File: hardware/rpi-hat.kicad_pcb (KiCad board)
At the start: 2 copper layers, 65 x 56 mm, 86 parts, among them J1 Conn_02x20_Odd_Even__Rpi, J10 A1, J11 A2, J12 A3, J13 A4, J14 A5, J15 Alert, J16 Conn_01x02_Male, J16 I2C 5V, J17 PPS, J2 USART, J3 Jumper, J4 Fan 1, J5 Fan 2, J6 I2C 3.3V, J7 10103594-0001LF, J8 I2C 3.3V, J9 A0, U1 EEPROM, U10 5V, U11 3.3V -> 5V, U2 FAN, U3 BUF, U4 BSS138, U5 BSS138, U6 BUF, U7 DAC, U8 MUX, U9 ADC

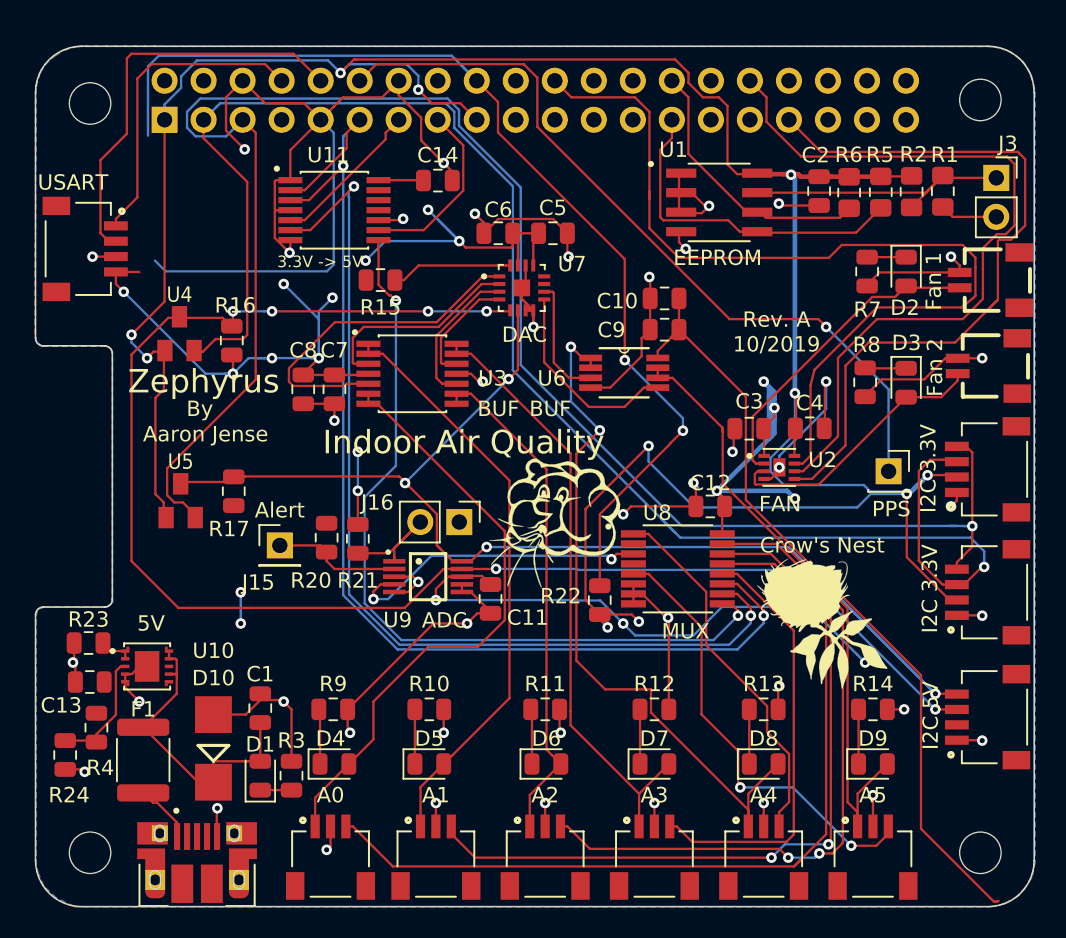
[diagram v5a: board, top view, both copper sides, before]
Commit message: Update silk screen
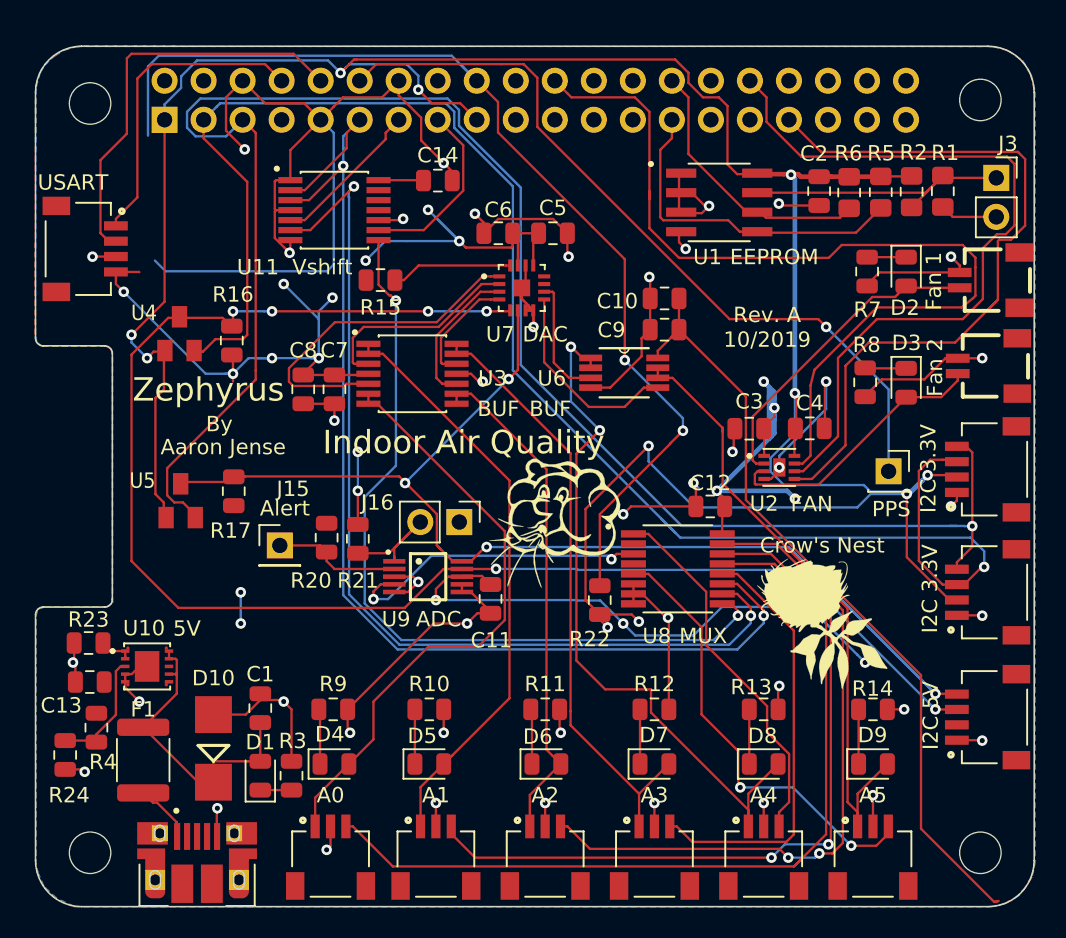
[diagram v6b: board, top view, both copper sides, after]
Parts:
- U11: value 3.3V -> 5V -> Vshift
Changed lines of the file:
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@@
   (layers
     (0 F.Cu signal hide)
-    (31 B.Cu signal hide)
+    (31 B.Cu signal)
     (32 B.Adhes user)
     (33 F.Adhes user)
-    (34 B.Paste user hide)
+    (34 B.Paste user)
     (35 F.Paste user)
     (36 B.SilkS user hide)
@@
     (at 209.4484 123.5788)
     (attr smd)
-    (fp_text reference U5 (at 0 -2.54) (layer F.SilkS)
+    (fp_text reference U5 (at -2.4892 -1.3032) (layer F.SilkS)
       (effects (font (size 1 0.9) (thickness 0.15)))
     )
@@
     (at 244.5004 104.1654)
     (attr smd)
-    (fp_text reference U1 (at -2.9718 -3.429) (layer F.SilkS)
+    (fp_text reference U1 (at -0.762 3.556) (layer F.SilkS)
       (effects (font (size 1 1) (thickness 0.15)))
     )
-    (fp_text value EEPROM (at -0.1016 3.6068) (layer F.SilkS)
+    (fp_text value EEPROM (at 3.5814 3.556) (layer F.SilkS)
       (effects (font (size 1 1) (thickness 0.15)))
     )
@@
     (at 248.412 121.412)
     (attr smd)
-    (fp_text reference U2 (at 2.8194 -0.4826) (layer F.SilkS)
+    (fp_text reference U2 (at -0.9906 2.3622) (layer F.SilkS)
       (effects (font (size 1 1) (thickness 0.15)))
     )
-    (fp_text value FAN (at 0.0508 2.3876) (layer F.SilkS)
+    (fp_text value FAN (at 2.1082 2.3876) (layer F.SilkS)
       (effects (font (size 1 1) (thickness 0.15)))
     )
@@
     (at 209.3722 112.7076)
     (attr smd)
-    (fp_text reference U4 (at 0 -2.54) (layer F.SilkS)
+    (fp_text reference U4 (at -2.3114 -1.354) (layer F.SilkS)
       (effects (font (size 1 0.9) (thickness 0.15)))
     )
@@
     (tags resistor)
     (attr smd)
-    (fp_text reference R17 (at -2.4638 -0.3048 180) (layer F.SilkS)
+    (fp_text reference R17 (at -2.5654 -0.2032 180) (layer F.SilkS)
       (effects (font (size 1 1) (thickness 0.15)))
     )
@@
     (tags resistor)
     (attr smd)
-    (fp_text reference R16 (at 2.2837 0.2286 180) (layer F.SilkS)
+    (fp_text reference R16 (at 2.9949 0.0762 180) (layer F.SilkS)
       (effects (font (size 1 1) (thickness 0.15)))
     )
@@
     (tags "resistor handsolder")
     (attr smd)
-    (fp_text reference R6 (at -2.4548 0.0254 180) (layer F.SilkS)
+    (fp_text reference R6 (at -2.5564 0.0508 180) (layer F.SilkS)
       (effects (font (size 1 1) (thickness 0.15)))
     )
@@
     (tags "resistor handsolder")
     (attr smd)
-    (fp_text reference R5 (at -2.4294 0.0508 180) (layer F.SilkS)
+    (fp_text reference R5 (at -2.531 -0.0254 180) (layer F.SilkS)
       (effects (font (size 1 1) (thickness 0.15)))
     )
@@
     (tags "resistor handsolder")
     (attr smd)
-    (fp_text reference R2 (at 2.3966 -1.905 180) (layer F.SilkS)
+    (fp_text reference R2 (at 2.5236 -1.905 180) (layer F.SilkS)
       (effects (font (size 1 1) (thickness 0.15)))
     )
@@
     (tags "resistor handsolder")
     (attr smd)
-    (fp_text reference R1 (at -2.3966 -2.159 180) (layer F.SilkS)
+    (fp_text reference R1 (at -2.5236 -2.1844 180) (layer F.SilkS)
       (effects (font (size 1 1) (thickness 0.15)))
     )
@@
     (tags capacitor)
     (attr smd)
-    (fp_text reference C2 (at -2.3345 0.2286 180) (layer F.SilkS)
+    (fp_text reference C2 (at -2.4361 0.3302 180) (layer F.SilkS)
       (effects (font (size 1 1) (thickness 0.15)))
     )
@@
     (at 219.457 104.668)
     (attr smd)
-    (fp_text reference U11 (at -0.41042 -3.58362) (layer F.SilkS)
+    (fp_text reference U11 (at -4.9794 3.7138) (layer F.SilkS)
       (effects (font (size 1 1) (thickness 0.15)))
     )
-    (fp_text value "3.3V -> 5V" (at -0.9408 3.3582) (layer F.SilkS)
-      (effects (font (size 0.75 0.75) (thickness 0.15)))
+    (fp_text value Vshift (at -0.7884 3.7138) (layer F.SilkS)
+      (effects (font (size 1 1) (thickness 0.15)))
     )
     (fp_line (start -4 2.75) (end -4 -2.75) (layer Eco1.User) (width 0.05))
@@
     (at 207.264 134.366)
     (attr smd)
-    (fp_text reference U10 (at 4.318 -1.016) (layer F.SilkS)
+    (fp_text reference U10 (at -0.2032 -2.4892) (layer F.SilkS)
       (effects (font (size 1 1) (thickness 0.15)))
     )
-    (fp_text value 5V (at 0.254 -2.794) (layer F.SilkS)
+    (fp_text value 5V (at 2.5908 -2.4638) (layer F.SilkS)
       (effects (font (size 1 1) (thickness 0.15)))
     )
@@
     (tags resistor)
     (attr smd)
-    (fp_text reference R4 (at 2.6185 -0.254 180) (layer F.SilkS)
+    (fp_text reference R4 (at 2.2375 -0.4318 180) (layer F.SilkS)
       (effects (font (size 1 1) (thickness 0.15)))
     )
@@
     (tags resistor)
     (attr smd)
-    (fp_text reference R3 (at 2.286 0 180) (layer F.SilkS)
+    (fp_text reference R3 (at 2.2606 0.0762 180) (layer F.SilkS)
       (effects (font (size 1 1) (thickness 0.15)))
     )
@@
     (tags diode)
     (attr smd)
-    (fp_text reference D1 (at 2.032 0 180) (layer F.SilkS)
+    (fp_text reference D1 (at 2.1844 0 180) (layer F.SilkS)
       (effects (font (size 1 1) (thickness 0.15)))
     )
@@
     (at 225.552 128.524)
     (attr smd)
-    (fp_text reference U9 (at -1.9812 2.8194) (layer F.SilkS)
+    (fp_text reference U9 (at -2.0828 2.7686) (layer F.SilkS)
       (effects (font (size 1 1) (thickness 0.15)))
     )
-    (fp_text value ADC (at 1.0668 2.8448) (layer F.SilkS)
+    (fp_text value ADC (at 0.6858 2.7686) (layer F.SilkS)
       (effects (font (size 1 1) (thickness 0.15)))
     )
@@
     (at 241.808 128.016)
     (attr smd)
-    (fp_text reference U8 (at -1.34 -3.647) (layer F.SilkS)
+    (fp_text reference U8 (at -1.3716 4.3688) (layer F.SilkS)
       (effects (font (size 1 1) (thickness 0.15)))
     )
-    (fp_text value MUX (at 0.508 4.064) (layer F.SilkS)
+    (fp_text value MUX (at 1.651 4.3688) (layer F.SilkS)
       (effects (font (size 1 1) (thickness 0.15)))
     )
@@
     (at 231.648 109.728)
     (attr smd)
-    (fp_text reference U7 (at 3.2766 -1.5494) (layer F.SilkS)
+    (fp_text reference U7 (at -1.397 3.0226) (layer F.SilkS)
       (effects (font (size 1 1) (thickness 0.15)))
     )
-    (fp_text value DAC (at 0.1778 3.048) (layer F.SilkS)
+    (fp_text value DAC (at 1.524 3.0226) (layer F.SilkS)
       (effects (font (size 1 1) (thickness 0.15)))
     )
@@
     (tags resistor)
     (attr smd)
-    (fp_text reference R22 (at 0.254 -2.54 180) (layer F.SilkS)
+    (fp_text reference R22 (at -2.54 -0.6604 180) (layer F.SilkS)
       (effects (font (size 1 1) (thickness 0.15)))
     )
@@
     (tags resistor)
     (attr smd)
-    (fp_text reference R14 (at 0 -1.65) (layer F.SilkS)
+    (fp_text reference R14 (at -0.0254 -1.3462) (layer F.SilkS)
       (effects (font (size 1 1) (thickness 0.15)))
     )
@@
     (tags resistor)
     (attr smd)
-    (fp_text reference R13 (at 0 -1.65) (layer F.SilkS)
+    (fp_text reference R13 (at -0.8128 -1.4478) (layer F.SilkS)
       (effects (font (size 1 1) (thickness 0.15)))
     )
@@
     (descr "Through hole straight pin header, 1x01, 2.54mm pitch, single row")
     (tags "Through hole pin header THT 1x01 2.54mm single row")
-    (fp_text reference J15 (at -1.397 2.413) (layer F.SilkS)
+    (fp_text reference J15 (at 0.8636 -3.683) (layer F.SilkS)
       (effects (font (size 1 1) (thickness 0.15)))
     )
@@
     (tags diode)
     (attr smd)
-    (fp_text reference D9 (at 0 -1.65) (layer F.SilkS)
+    (fp_text reference D9 (at -0.0254 -1.8796) (layer F.SilkS)
       (effects (font (size 1 1) (thickness 0.15)))
     )
@@
     (tags diode)
     (attr smd)
-    (fp_text reference D8 (at 0 -1.65) (layer F.SilkS)
+    (fp_text reference D8 (at -0.0762 -1.8288) (layer F.SilkS)
       (effects (font (size 1 1) (thickness 0.15)))
     )
@@
     (tags diode)
     (attr smd)
-    (fp_text reference D7 (at 0 -1.65) (layer F.SilkS)
+    (fp_text reference D7 (at -0.0254 -1.8796) (layer F.SilkS)
       (effects (font (size 1 1) (thickness 0.15)))
     )
@@
     (tags diode)
     (attr smd)
-    (fp_text reference D6 (at 0 -1.65) (layer F.SilkS)
+    (fp_text reference D6 (at -0.5611 -1.778) (layer F.SilkS)
       (effects (font (size 1 1) (thickness 0.15)))
     )
@@
     (tags diode)
     (attr smd)
-    (fp_text reference D5 (at 0 -1.65) (layer F.SilkS)
+    (fp_text reference D5 (at -0.4595 -1.8288) (layer F.SilkS)
       (effects (font (size 1 1) (thickness 0.15)))
     )
@@
     (tags diode)
     (attr smd)
-    (fp_text reference D4 (at -0.254 -1.65) (layer F.SilkS)
+    (fp_text reference D4 (at -0.3048 -1.9304) (layer F.SilkS)
       (effects (font (size 1 1) (thickness 0.15)))
     )
@@
     (tags capacitor)
     (attr smd)
-    (fp_text reference C11 (at 1.2215 -2.413 180) (layer F.SilkS)
+    (fp_text reference C11 (at 2.6947 -0.0508 180) (layer F.SilkS)
       (effects (font (size 1 1) (thickness 0.15)))
     )
@@
     )
   )
-  (gr_text "Rev. A\n10/2019" (at 248.2342 112.5982) (layer F.SilkS)
+  (gr_text "Rev. A\n10/2019" (at 247.6246 112.2934) (layer F.SilkS)
     (effects (font (size 1 1) (thickness 0.25)))
   )
@@
     (effects (font (size 1.4 1.4) (thickness 0.35)) (justify mirror))
   )
-  (gr_text Zephyrus (at 210.947 115.824) (layer F.SilkS)
+  (gr_text Zephyrus (at 211.2518 116.3574) (layer F.SilkS)
     (effects (font (size 1.524 1.524) (thickness 0.3)))
   )
-  (gr_text "Aaron Jense" (at 211.074 119.253) (layer F.SilkS)
+  (gr_text "Aaron Jense" (at 212.217 120.0912) (layer F.SilkS)
     (effects (font (size 1 1) (thickness 0.25)))
   )
-  (gr_text By (at 210.693 117.602) (layer F.SilkS)
+  (gr_text By (at 211.963 118.5926) (layer F.SilkS)
     (effects (font (size 1 1) (thickness 0.25)))
   )
@@
     (effects (font (size 1.524 1.524) (thickness 0.3)))
   )
-  (gr_text Alert (at 215.9 124.206) (layer F.SilkS)
+  (gr_text Alert (at 216.2302 124.079) (layer F.SilkS)
     (effects (font (size 1 1) (thickness 0.15)))
   )

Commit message: Hardware changes for PCB order 1
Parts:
- removed R22: 10K, Resistor_SMD:R_0805_2012Metric
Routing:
- net /GPIO24(GEN5): track 69.2 -> 0.00 mm, vias 2 -> 0
- net +3V3: track 180.9 -> 146.9 mm, vias 11 -> 8
- net /Analog_Sensors/BUF_OUT_4: track 47.0 -> 44.0 mm
- net +5V: vias 20 -> 19
